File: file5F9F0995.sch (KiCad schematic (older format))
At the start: 1 part, among them J1 ATX-24

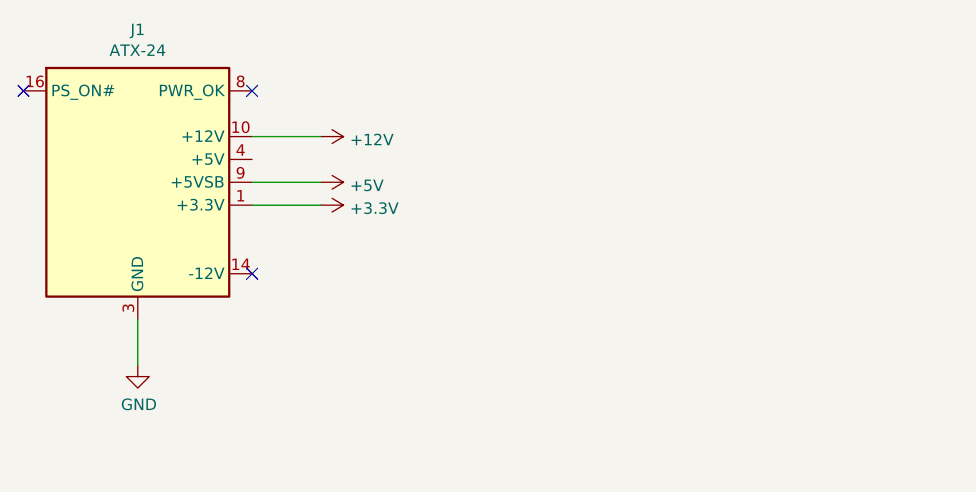
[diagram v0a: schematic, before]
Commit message: Added footprints
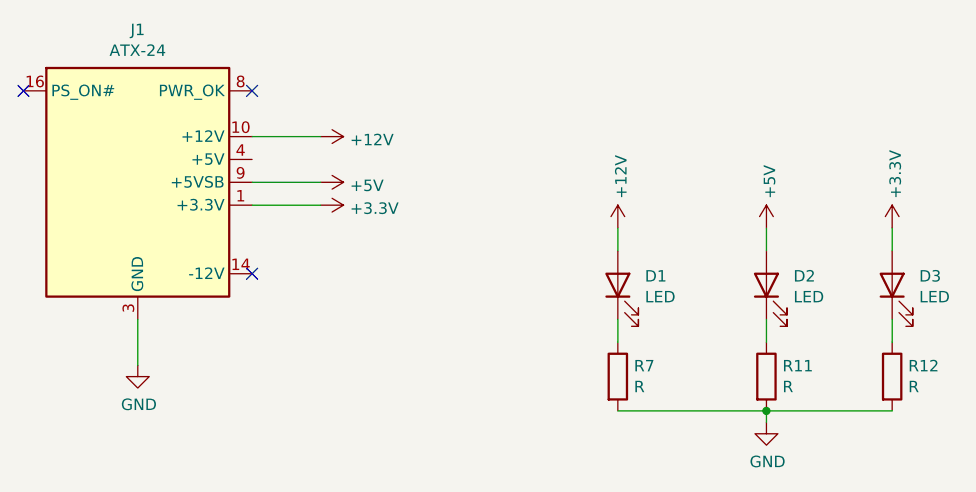
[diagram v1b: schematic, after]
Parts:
- added D1, D2, D3: LED, LED_SMD:LED_0805_2012Metric, symbol Device:LED
- added R11, R12, R7: R, Resistor_SMD:R_0805_2012Metric, symbol Device:R
- J1: footprint (none) -> Connector_Molex:Molex_Mini-Fit_Jr_5566-24A_2x12_P4.20mm_Vertical
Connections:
- net +12V: now also D1.2 (A)
- net +3V3: now also D3.2 (A)
- net +5V: now also D2.2 (A)
- net GND: now also R11.2, R12.2, R7.2
- new net: D1.1 (K), R7.1
- new net: D2.1 (K), R11.1
- new net: D3.1 (K), R12.1
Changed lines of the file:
@@
 F 0 "J1" H 2500 2067 50  0000 C CNN
 F 1 "ATX-24" H 2500 1976 50  0000 C CNN
-F 2 "" H 2500 1300 50  0001 C CNN
+F 2 "Connector_Molex:Molex_Mini-Fit_Jr_5566-24A_2x12_P4.20mm_Vertical" H 2500 1300 50  0001 C CNN
 F 3 "https://www.intel.com/content/dam/www/public/us/en/documents/guides/power-supply-design-guide-june.pdf#page=33" H 4900 850 50  0001 C CNN
 	1    2500 1400
@@
 NoConn ~ 3000 1000
 NoConn ~ 2000 1000
+$Comp
+L power:GND #PWR038
+U 1 1 5FA374FD
+P 5250 2450
+F 0 "#PWR038" H 5250 2200 50  0001 C CNN
+F 1 "GND" H 5255 2277 50  0000 C CNN
+F 2 "" H 5250 2450 50  0001 C CNN
+F 3 "" H 5250 2450 50  0001 C CNN
+	1    5250 2450
+	1    0    0    -1
+$EndComp
+$Comp
+L power:+12V #PWR035
+U 1 1 5FA37A64
+P 4600 1600
+F 0 "#PWR035" H 4600 1450 50  0001 C CNN
+F 1 "+12V" V 4615 1728 50  0000 L CNN
+F 2 "" H 4600 1600 50  0001 C CNN
+F 3 "" H 4600 1600 50  0001 C CNN
+	1    4600 1600
+	1    0    0    -1
+$EndComp
+$Comp
+L power:+5V #PWR036
+U 1 1 5FA385B0
+P 5250 1600
+F 0 "#PWR036" H 5250 1450 50  0001 C CNN
+F 1 "+5V" V 5265 1728 50  0000 L CNN
+F 2 "" H 5250 1600 50  0001 C CNN
+F 3 "" H 5250 1600 50  0001 C CNN
+	1    5250 1600
+	1    0    0    -1
+$EndComp
+$Comp
+L power:+3.3V #PWR039
+U 1 1 5FA39069
+P 5800 1600
+F 0 "#PWR039" H 5800 1450 50  0001 C CNN
+F 1 "+3.3V" V 5815 1728 50  0000 L CNN
+F 2 "" H 5800 1600 50  0001 C CNN
+F 3 "" H 5800 1600 50  0001 C CNN
+	1    5800 1600
+	1    0    0    -1
+$EndComp
+$Comp
+L Device:R R7
+U 1 1 5FA3A71A
+P 4600 2250
+F 0 "R7" H 4670 2296 50  0000 L CNN
+F 1 "R" H 4670 2205 50  0000 L CNN
+F 2 "Resistor_SMD:R_0805_2012Metric" V 4530 2250 50  0001 C CNN
+F 3 "~" H 4600 2250 50  0001 C CNN
+	1    4600 2250
+	1    0    0    -1
+$EndComp
+$Comp
+L Device:R R11
+U 1 1 5FA3AB36
+P 5250 2250
+F 0 "R11" H 5320 2296 50  0000 L CNN
+F 1 "R" H 5320 2205 50  0000 L CNN
+F 2 "Resistor_SMD:R_0805_2012Metric" V 5180 2250 50  0001 C CNN
+F 3 "~" H 5250 2250 50  0001 C CNN
+	1    5250 2250
+	1    0    0    -1
+$EndComp
+$Comp
+L Device:R R12
+U 1 1 5FA3B8DA
+P 5800 2250
+F 0 "R12" H 5870 2296 50  0000 L CNN
+F 1 "R" H 5870 2205 50  0000 L CNN
+F 2 "Resistor_SMD:R_0805_2012Metric" V 5730 2250 50  0001 C CNN
+F 3 "~" H 5800 2250 50  0001 C CNN
+	1    5800 2250
+	1    0    0    -1
+$EndComp
+$Comp
+L Device:LED D1
+U 1 1 5FA3D0CA
+P 4600 1850
+F 0 "D1" V 4639 1732 50  0000 R CNN
+F 1 "LED" V 4548 1732 50  0000 R CNN
+F 2 "LED_SMD:LED_0805_2012Metric" H 4600 1850 50  0001 C CNN
+F 3 "~" H 4600 1850 50  0001 C CNN
+	1    4600 1850
+	0    -1   -1   0
+$EndComp
+$Comp
+L Device:LED D2
+U 1 1 5FA3DAE9
+P 5250 1850
+F 0 "D2" V 5289 1732 50  0000 R CNN
+F 1 "LED" V 5198 1732 50  0000 R CNN
+F 2 "LED_SMD:LED_0805_2012Metric" H 5250 1850 50  0001 C CNN
+F 3 "~" H 5250 1850 50  0001 C CNN
+	1    5250 1850
+	0    -1   -1   0
+$EndComp
+$Comp
+L Device:LED D3
+U 1 1 5FA3DD50
+P 5800 1850
+F 0 "D3" V 5839 1732 50  0000 R CNN
+F 1 "LED" V 5748 1732 50  0000 R CNN
+F 2 "LED_SMD:LED_0805_2012Metric" H 5800 1850 50  0001 C CNN
+F 3 "~" H 5800 1850 50  0001 C CNN
+	1    5800 1850
+	0    -1   -1   0
+$EndComp
+Wire Wire Line
+	5800 1600 5800 1700
+Wire Wire Line
+	5800 2000 5800 2100
+Wire Wire Line
+	5250 2000 5250 2100
+Wire Wire Line
+	5250 1700 5250 1600
+Wire Wire Line
+	4600 1700 4600 1600
+Wire Wire Line
+	4600 2000 4600 2100
+Wire Wire Line
+	4600 2400 5250 2400
+Connection ~ 5250 2400
+Wire Wire Line
+	5250 2400 5800 2400
+Wire Wire Line
+	5250 2400 5250 2450
 $EndSCHEMATC

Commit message: Placement
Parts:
- R11, R12, R7: value R -> 1k
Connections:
- net GND: now also R12.1; no longer R12.2
- net at D3.1 (K): now also R12.2; no longer R12.1
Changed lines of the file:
@@
 P 4600 2250
 F 0 "R7" H 4670 2296 50  0000 L CNN
-F 1 "R" H 4670 2205 50  0000 L CNN
+F 1 "1k" H 4670 2205 50  0000 L CNN
 F 2 "Resistor_SMD:R_0805_2012Metric" V 4530 2250 50  0001 C CNN
 F 3 "~" H 4600 2250 50  0001 C CNN
@@
 P 5250 2250
 F 0 "R11" H 5320 2296 50  0000 L CNN
-F 1 "R" H 5320 2205 50  0000 L CNN
+F 1 "1k" H 5320 2205 50  0000 L CNN
 F 2 "Resistor_SMD:R_0805_2012Metric" V 5180 2250 50  0001 C CNN
 F 3 "~" H 5250 2250 50  0001 C CNN
@@
 P 5800 2250
 F 0 "R12" H 5870 2296 50  0000 L CNN
-F 1 "R" H 5870 2205 50  0000 L CNN
+F 1 "1k" H 5870 2205 50  0000 L CNN
 F 2 "Resistor_SMD:R_0805_2012Metric" V 5730 2250 50  0001 C CNN
 F 3 "~" H 5800 2250 50  0001 C CNN
 	1    5800 2250
-	1    0    0    -1
+	1    0    0    1
 $EndComp
 $Comp

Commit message: Trackeo
Pobre trackeo parcial. Backup
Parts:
- R7: value 1k -> 10k
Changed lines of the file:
@@
 P 4600 2250
 F 0 "R7" H 4670 2296 50  0000 L CNN
-F 1 "1k" H 4670 2205 50  0000 L CNN
+F 1 "10k" H 4670 2205 50  0000 L CNN
 F 2 "Resistor_SMD:R_0805_2012Metric" V 4530 2250 50  0001 C CNN
 F 3 "~" H 4600 2250 50  0001 C CNN

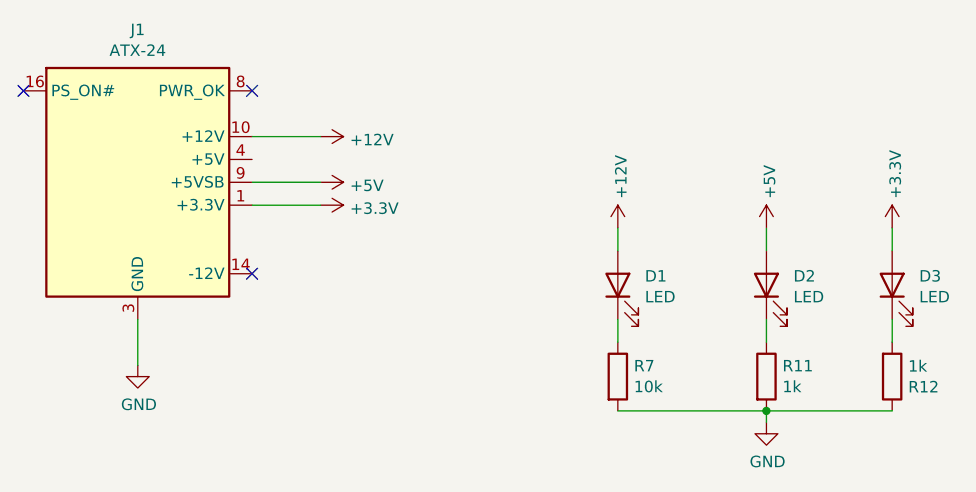
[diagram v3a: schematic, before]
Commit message: Removal of LED 5V and further routing
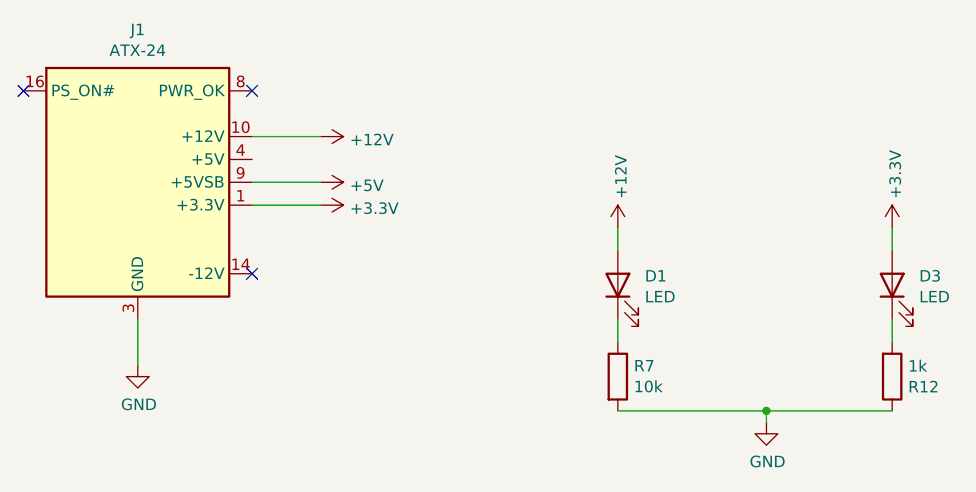
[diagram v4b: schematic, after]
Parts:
- removed D2: LED, LED_SMD:LED_0805_2012Metric, symbol Device:LED
- removed R11: 1k, Resistor_SMD:R_0805_2012Metric, symbol Device:R
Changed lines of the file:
@@
-$EndComp
-$Comp
-L power:+5V #PWR036
-U 1 1 5FA385B0
-P 5250 1600
-F 0 "#PWR036" H 5250 1450 50  0001 C CNN
-F 1 "+5V" V 5265 1728 50  0000 L CNN
-F 2 "" H 5250 1600 50  0001 C CNN
-F 3 "" H 5250 1600 50  0001 C CNN
-	1    5250 1600
-	1    0    0    -1
 $EndComp
 $Comp
@@
 F 3 "~" H 4600 2250 50  0001 C CNN
 	1    4600 2250
-	1    0    0    -1
-$EndComp
-$Comp
-L Device:R R11
-U 1 1 5FA3AB36
-P 5250 2250
-F 0 "R11" H 5320 2296 50  0000 L CNN
-F 1 "1k" H 5320 2205 50  0000 L CNN
-F 2 "Resistor_SMD:R_0805_2012Metric" V 5180 2250 50  0001 C CNN
-F 3 "~" H 5250 2250 50  0001 C CNN
-	1    5250 2250
 	1    0    0    -1
 $EndComp
@@
 $EndComp
 $Comp
-L Device:LED D2
-U 1 1 5FA3DAE9
-P 5250 1850
-F 0 "D2" V 5289 1732 50  0000 R CNN
-F 1 "LED" V 5198 1732 50  0000 R CNN
-F 2 "LED_SMD:LED_0805_2012Metric" H 5250 1850 50  0001 C CNN
-F 3 "~" H 5250 1850 50  0001 C CNN
-	1    5250 1850
-	0    -1   -1   0
-$EndComp
-$Comp
 L Device:LED D3
 U 1 1 5FA3DD50
@@
 	5800 2000 5800 2100
 Wire Wire Line
-	5250 2000 5250 2100
-Wire Wire Line
-	5250 1700 5250 1600
-Wire Wire Line
 	4600 1700 4600 1600
